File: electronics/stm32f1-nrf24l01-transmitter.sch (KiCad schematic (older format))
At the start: 29 parts, among them K1 CONN_3, K10 CONN_3, K11 CONN_3, K2 CONN_3, K3 CONN_3, K4 CONN_3, K5 CONN_3, K6 CONN_3, K7 CONN_3, K8 CONN_3, K9 CONN_3, P1 Charge, P2 LED, P3 CONN_2, P4 CONN_2, P5 CONN_4, Q1 BC548, SW1 ON/OFF, U1 LIPO_CHARGER_+_PROTECTION, U2 STM32F103C8T6_DEV_BOARD, U3 NRF24L01P

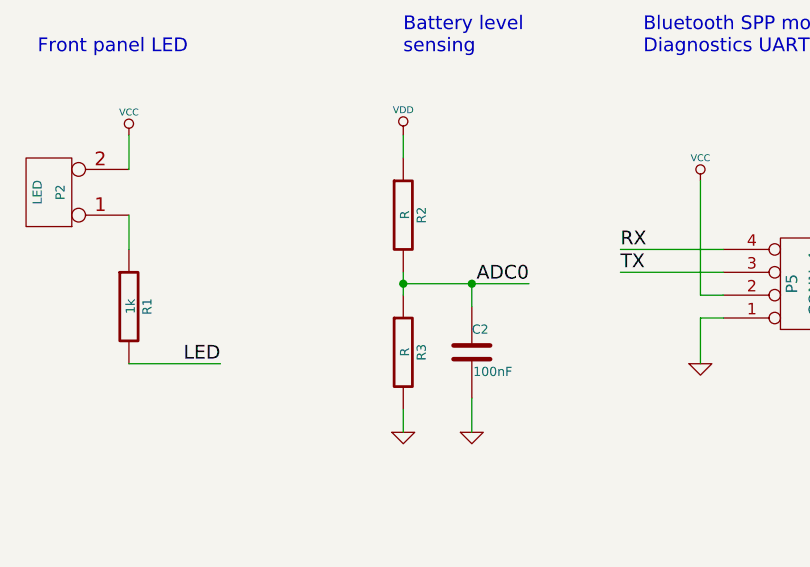
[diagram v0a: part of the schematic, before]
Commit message: Define values for battery voltage divider
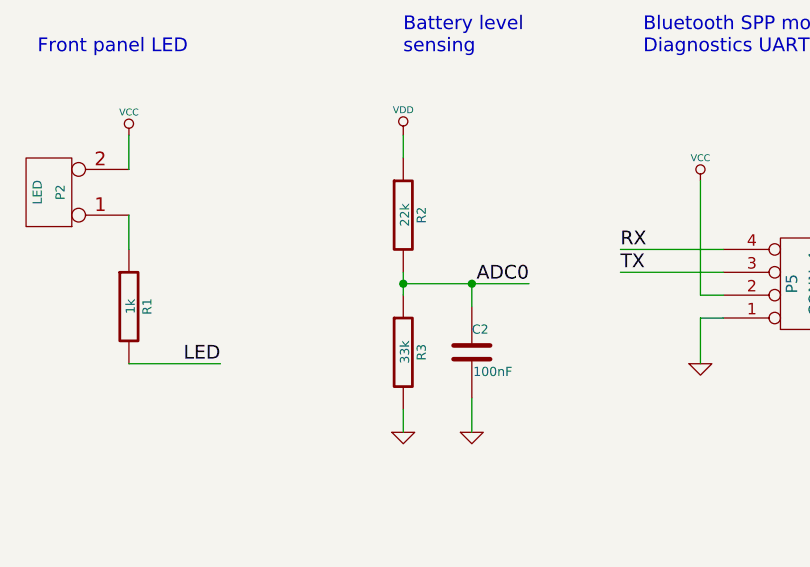
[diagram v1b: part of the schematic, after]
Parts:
- R2: value R -> 22k
- R3: value R -> 33k
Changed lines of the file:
@@
 EESchema Schematic File Version 2
+LIBS:WLA-STM32
+LIBS:WLA-nrf24
+LIBS:WLA-power
 LIBS:power
 LIBS:device
@@
 Sheet 1 1
 Title "STM32F1 NRF24L01 RC transmitter"
-Date "12 jun 2016"
+Date "19 jun 2016"
 Rev "1"
 Comp "LANE Boys RC"
@@
 P 8800 5900
 F 0 "R2" V 8880 5900 40  0000 C CNN
-F 1 "R" V 8807 5901 40  0000 C CNN
+F 1 "22k" V 8807 5901 40  0000 C CNN
 F 2 "~" V 8730 5900 30  0000 C CNN
 F 3 "~" H 8800 5900 30  0000 C CNN
@@
 P 8800 6500
 F 0 "R3" V 8880 6500 40  0000 C CNN
-F 1 "R" V 8807 6501 40  0000 C CNN
+F 1 "33k" V 8807 6501 40  0000 C CNN
 F 2 "~" V 8730 6500 30  0000 C CNN
 F 3 "~" H 8800 6500 30  0000 C CNN

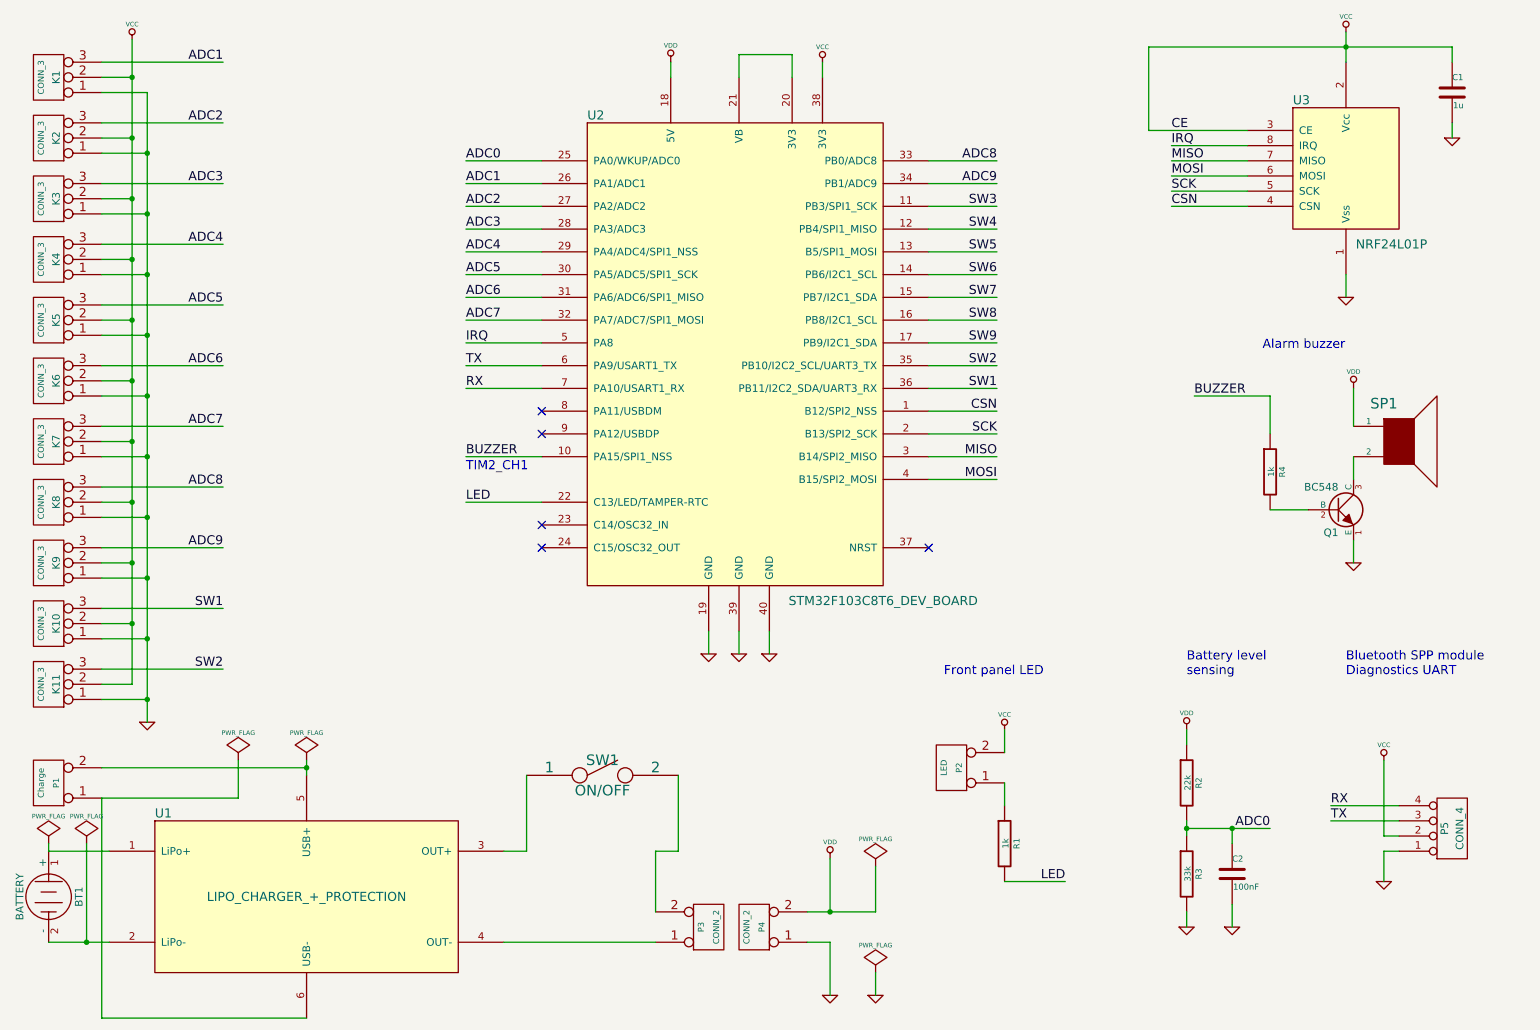
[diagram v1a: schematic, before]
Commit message: - Config: remove schematic reference, rather have schematic use pin names
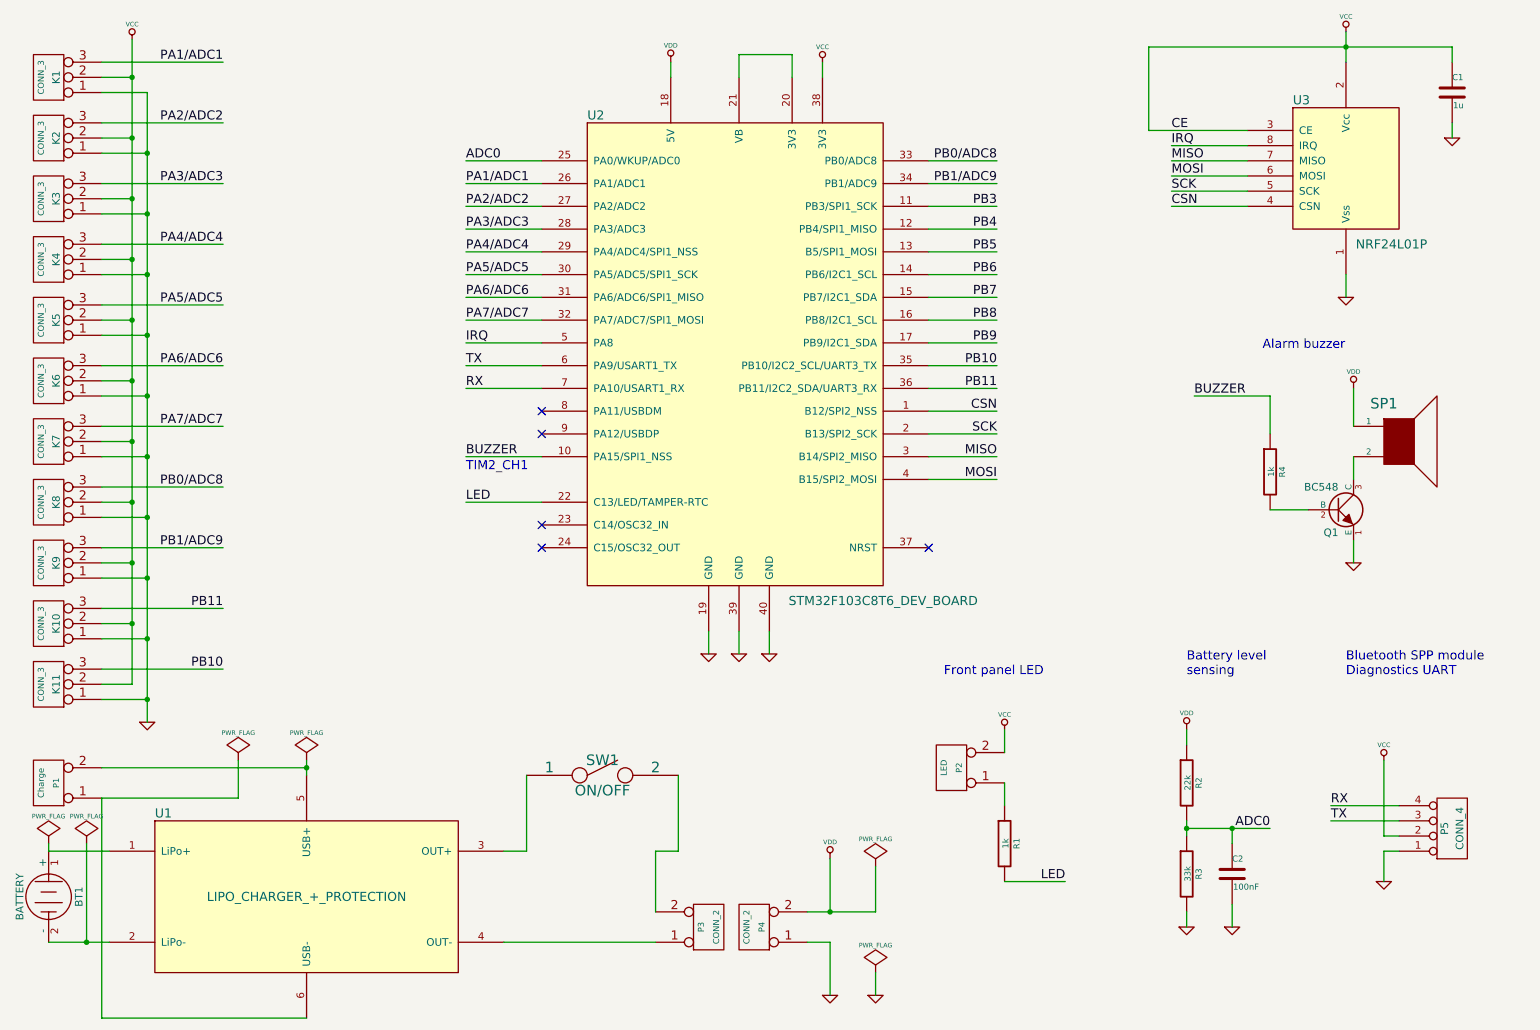
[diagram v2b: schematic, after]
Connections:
- net ADC1 renamed PA1/ADC1
- net ADC2 renamed PA2/ADC2
- net ADC3 renamed PA3/ADC3
- net ADC4 renamed PA4/ADC4
- net ADC5 renamed PA5/ADC5
- net ADC6 renamed PA6/ADC6
- net ADC7 renamed PA7/ADC7
- net ADC8 renamed PB0/ADC8
- net ADC9 renamed PB1/ADC9
- net SW1 renamed PB11
- net SW2 renamed PB10
- net SW3 renamed PB3
- net SW4 renamed PB4
- net SW5 renamed PB5
- net SW6 renamed PB6
- net SW7 renamed PB7
- net SW8 renamed PB8
- net SW9 renamed PB9
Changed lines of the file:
@@
 Sheet 1 1
 Title "STM32F1 NRF24L01 RC transmitter"
-Date "19 jun 2016"
+Date "11 aug 2016"
 Rev "1"
 Comp "LANE Boys RC"
@@
 ADC0
 Text Label 4050 1950 0    60   ~ 0
-ADC1
+PA1/ADC1
 Text Label 4050 2100 0    60   ~ 0
-ADC2
+PA2/ADC2
 Text Label 4050 2250 0    60   ~ 0
-ADC3
+PA3/ADC3
 Text Label 4050 2400 0    60   ~ 0
-ADC4
+PA4/ADC4
 Text Label 4050 2550 0    60   ~ 0
-ADC5
+PA5/ADC5
 Text Label 4050 2700 0    60   ~ 0
-ADC6
+PA6/ADC6
 Text Label 4050 2850 0    60   ~ 0
-ADC7
+PA7/ADC7
 Text Label 7550 1800 2    60   ~ 0
-ADC8
+PB0/ADC8
 Text Label 7550 1950 2    60   ~ 0
-ADC9
+PB1/ADC9
 Text Label 4050 3000 0    60   ~ 0
 IRQ
@@
 Connection ~ 1950 1750
 Text Label 2450 1150 2    60   ~ 0
-ADC1
+PA1/ADC1
 Text Label 2450 1550 2    60   ~ 0
-ADC2
+PA2/ADC2
 Text Label 2450 1950 2    60   ~ 0
-ADC3
+PA3/ADC3
 Text Label 2450 2350 2    60   ~ 0
-ADC4
+PA4/ADC4
 Text Label 2450 2750 2    60   ~ 0
-ADC5
+PA5/ADC5
 Text Label 2450 3150 2    60   ~ 0
-ADC6
+PA6/ADC6
 Text Label 2450 3550 2    60   ~ 0
-ADC7
+PA7/ADC7
 Text Label 2450 3950 2    60   ~ 0
-ADC8
+PB0/ADC8
 Text Label 2450 4350 2    60   ~ 0
-ADC9
+PB1/ADC9
 Text Label 2450 4750 2    60   ~ 0
-SW1
+PB11
 Text Label 2450 5150 2    60   ~ 0
-SW2
+PB10
 Wire Wire Line
 	7550 3300 7100 3300
@@
 	7550 3150 7100 3150
 Text Label 7550 3150 2    60   ~ 0
-SW2
+PB10
 Text Label 7550 3300 2    60   ~ 0
-SW1
+PB11
 $Comp
 L GND #PWR015
@@
 	7550 3000 7100 3000
 Text Label 7550 2100 2    60   ~ 0
-SW3
+PB3
 Text Label 7550 2250 2    60   ~ 0
-SW4
+PB4
 Text Label 7550 2400 2    60   ~ 0
-SW5
+PB5
 Text Label 7550 2550 2    60   ~ 0
-SW6
+PB6
 Text Label 7550 2700 2    60   ~ 0
-SW7
+PB7
 Text Label 7550 2850 2    60   ~ 0
-SW8
+PB8
 Text Label 7550 3000 2    60   ~ 0
-SW9
+PB9
 $EndSCHEMATC
